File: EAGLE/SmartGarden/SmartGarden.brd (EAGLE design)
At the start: 75 x 70 mm, 16 parts

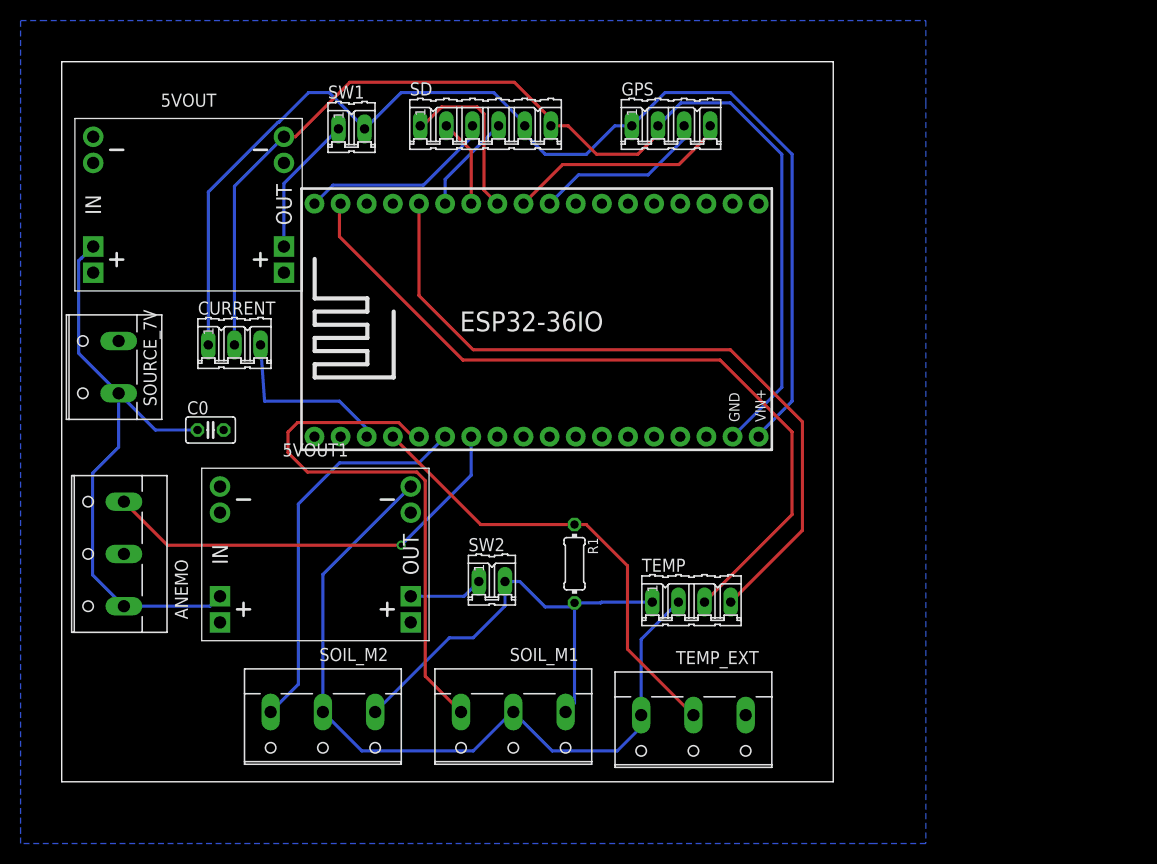
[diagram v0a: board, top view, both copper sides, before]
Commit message: Fix errors in PCB, added capacitors and holes
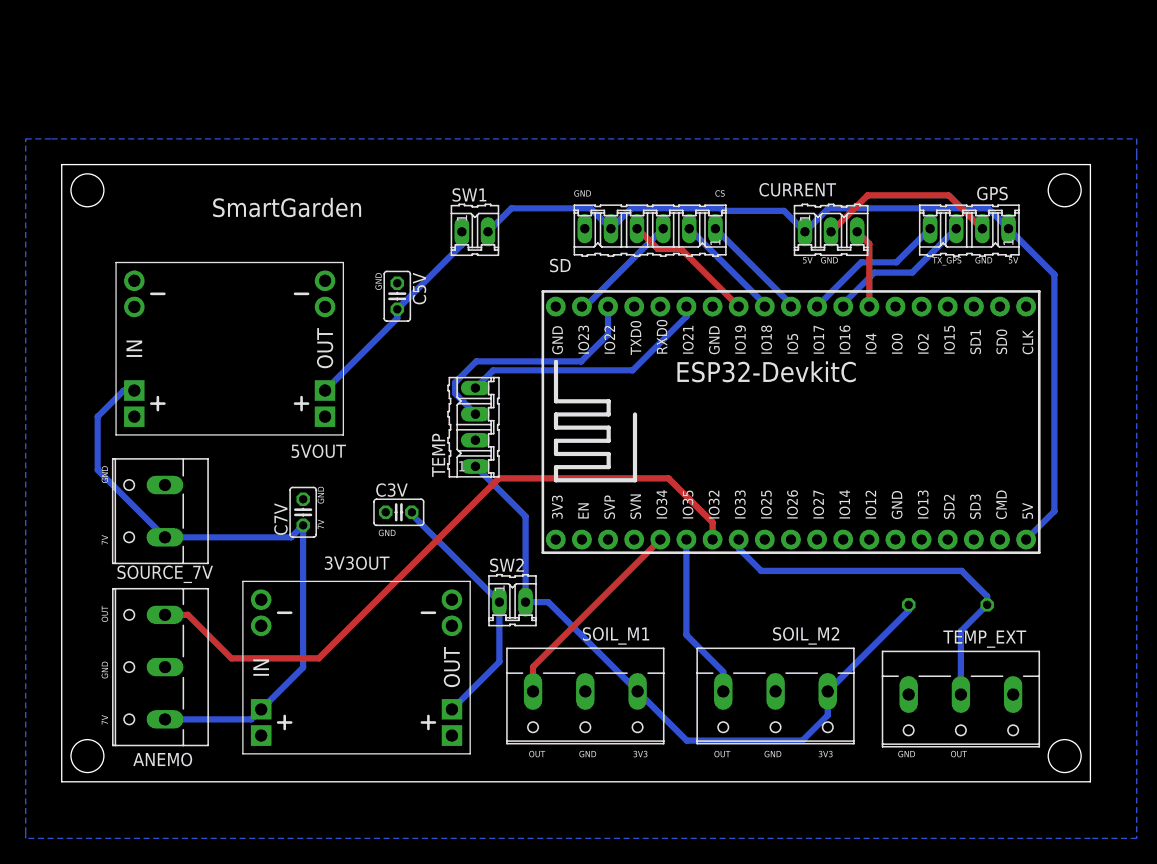
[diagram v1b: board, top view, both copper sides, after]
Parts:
- removed 5VOUT1: DC-DC-STEP-DOWN-MP1584, diy-modules:DC-DC-STEP-DOWN-MP1584
- removed C0: (no value), rcl:C025-025X050
- added 3V3OUT: DC-DC-STEP-DOWN-MP1584, diy-modules:DC-DC-STEP-DOWN-MP1584
- added C3V, C5V, C7V: (no value), rcl:C025-025X050
- ESP32: value ESP32-36IO -> ESP32DEVKITC; device ESP32:ESP32-36-GPIO -> ESP32:ESP32-DEVKITC
- moved CURRENT 59.0 mm to (74.8, 53.5)
- moved SOIL_M2 44.0 mm to (69.4, 8.15)
- moved R1 36.5 mm to (86.2, 17.2), flipped to the bottom, turned to 0 degrees
- moved GPS 30.7 mm to (88.2, 53.8), turned to 180 degrees
- moved TEMP 27.0 mm to (40.2, 34.5), turned to 90 degrees
- moved TEMP_EXT 26.1 mm to (87.4, 7.85)
- moved ESP32 25.5 mm to (70.9, 35.0)
- moved SD 18.9 mm to (57.2, 53.8), turned to 180 degrees
- moved SW1 15.6 mm to (40.2, 53.5)
- moved SOURCE_7V 14.7 mm to (9.40, 26.3)
- moved 5VOUT 14.6 mm to (16.3, 42.1)
- moved ANEMO 11.7 mm to (9.41, 11.2)
- moved SOIL_M1 7.28 mm to (50.9, 8.15)
- moved SW2 2.83 mm to (43.8, 17.5)
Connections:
- net RX renamed RX_GPS
- net TX renamed TX_GPS
- removed net CURRE: CURRENT.3, ESP32.3
- removed net N$1: 5VOUT.IN-.1
- removed net OUT3V-: 5VOUT1.OUT-.1, SOIL_M1.2, SOIL_M2.2, TEMP.2, TEMP_EXT.3
- removed net OUT5V-: 5VOUT.OUT-.1, CURRENT.2, ESP32.17, GPS.2, SD.6
- new net CURRENT: CURRENT.3, ESP32.26
- net 7V: now also 3V3OUT.IN+.1, C7V.1; no longer 5VOUT1.IN+.1, C0.1
- net GND: now also 3V3OUT.IN-.1, 3V3OUT.OUT-.1, 5VOUT.IN-.1, 5VOUT.OUT-.1, C3V.1, C5V.1, C7V.2, CURRENT.2, ESP32.14, GPS.2, SD.6, SOIL_M1.2, SOIL_M2.2, TEMP.2, TEMP_EXT.3; no longer 5VOUT.IN+.2, 5VOUT1.IN-.1, C0.2
- net MOSI: now also ESP32.37; no longer ESP32.36
- net N$2: now also 3V3OUT.OUT+.1, C3V.2; no longer 5VOUT1.OUT+.1
- net N$3: now also C5V.2
- net OUT5V+: now also ESP32.19; no longer ESP32.18
- net SCK: now also ESP32.36; no longer ESP32.35
- net SDA: now also ESP32.33; no longer ESP32.32
- net TEMP2: now also ESP32.8; no longer ESP32.4
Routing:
- net OUT5V-: track 110.2 -> 0.00 mm
- net OUT3V-: track 75.7 -> 0.00 mm
- net SCK: track 75.2 -> 23.4 mm
- net SDA: track 71.7 -> 24.4 mm
- net SOIL1: track 54.1 -> 19.9 mm
- net OUT5V+: track 115.4 -> 89.1 mm
- net ANEM: track 42.1 -> 65.7 mm, vias 1 -> 0
- net SOIL2: track 38.3 -> 16.2 mm
- net OUT3V+: track 45.6 -> 65.2 mm
- net GND: track 0.00 -> 17.5 mm
- net N$2: track 7.21 -> 24.6 mm
- net CURRE: track 17.3 -> 0.00 mm
- net MOSI: track 19.1 -> 11.0 mm
- net CURRENT: track 0.00 -> 7.76 mm
- net TEMP2: track 45.2 -> 37.5 mm
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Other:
- board size 75 x 70 mm -> 100 x 60 mm
- board text added: "/home/alejo/Downloads/PCB2(1).bmp"
- board text added: "3V3"
- board text added: "5V"
- board text added: "7V"
- board text added: "CS"
- board text added: "GND"
- board text added: "OUT"
- board text added: "SmartGarden"
- board text added: "TX_GPS"
